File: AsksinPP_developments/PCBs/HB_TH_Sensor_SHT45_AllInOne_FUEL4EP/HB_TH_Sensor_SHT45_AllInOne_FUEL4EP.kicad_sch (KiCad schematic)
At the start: 41 parts, among them J1 Conn_01x03, J2 FTDI Debuger, J3 ISP Programmer, SW1 Config button, U1 ATmega1284P-AU, U2 TPS61221DCK, U3 SHT45-AD1B-R2

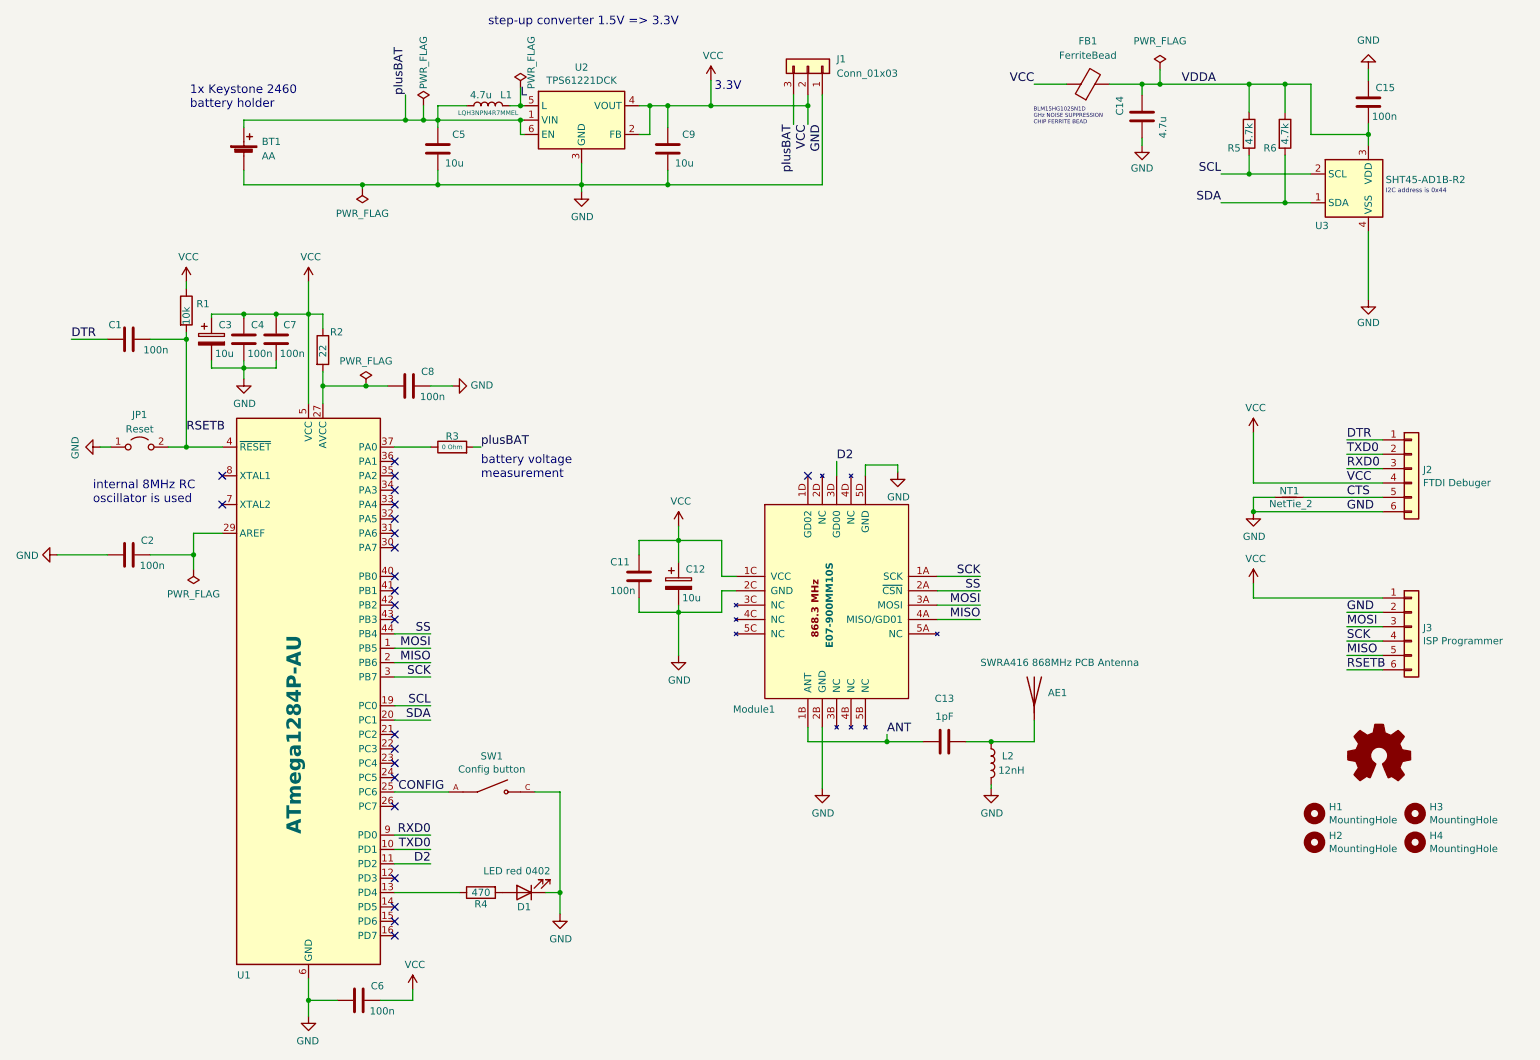
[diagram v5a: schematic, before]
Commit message: PCBs/HB_TH_Sensor_SHT45_AllInOne_FUEL4EP: Migration to KiCAD 8; improve solderability of RF module by hand
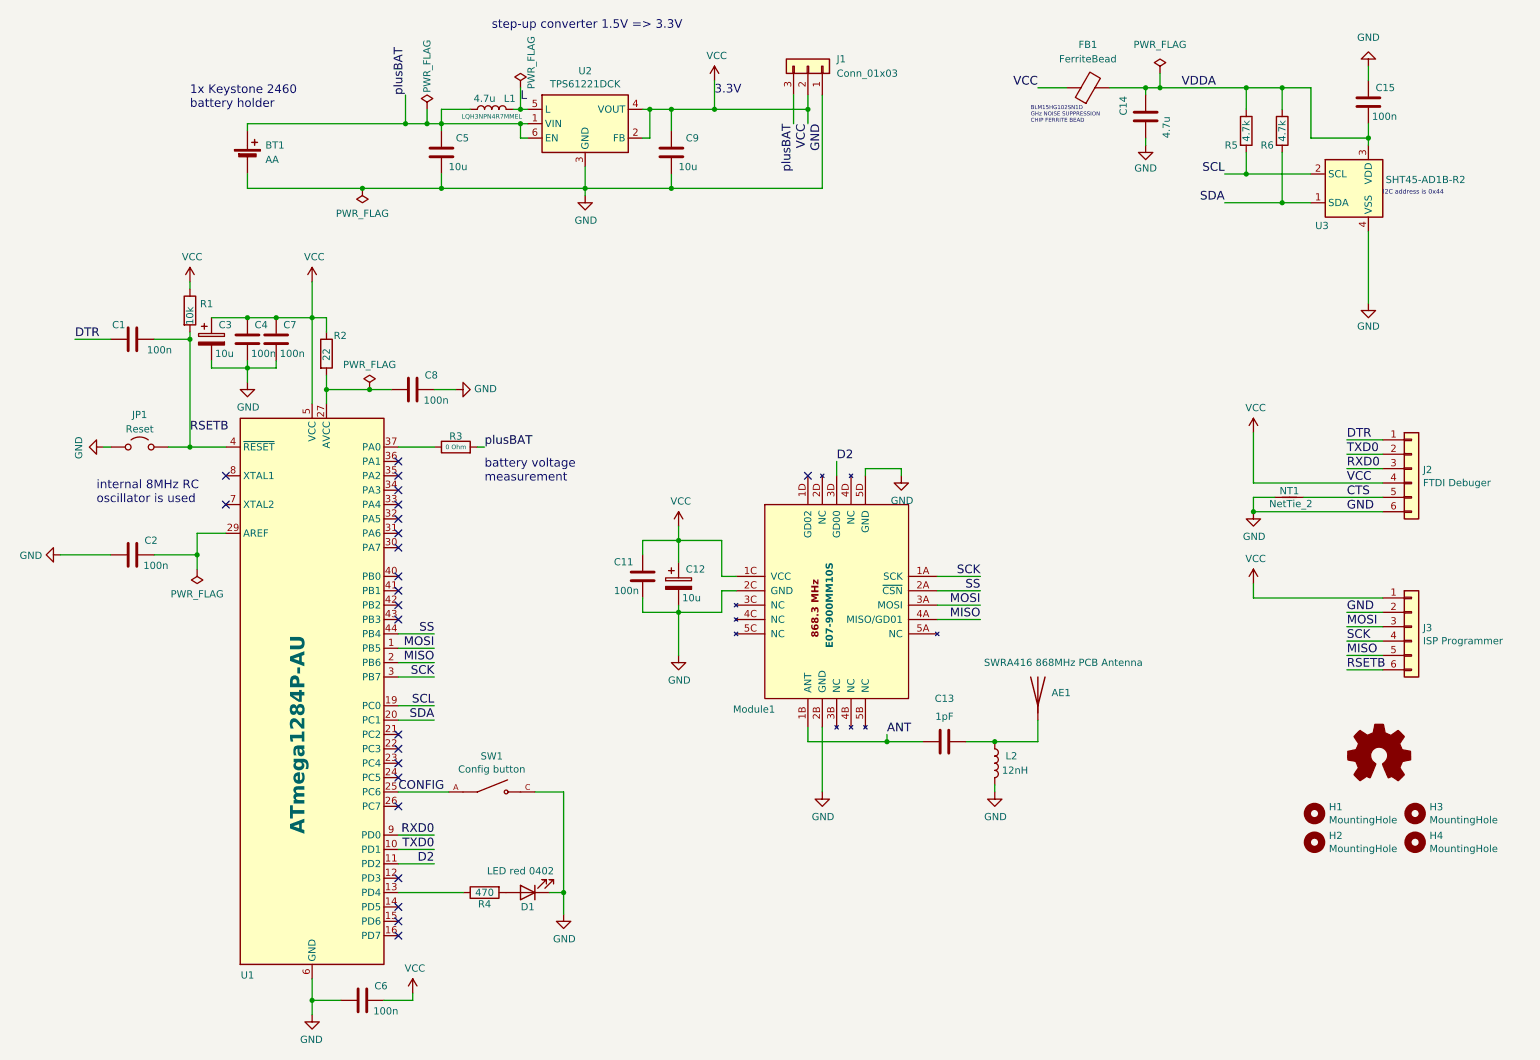
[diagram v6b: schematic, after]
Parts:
- AE1: footprint RF_Antenna:Texas_SWRA416_868MHz_915MHz -> FUEL4EP:Texas_SWRA416_868MHz_915MHz
- U3: footprint FUEL4EP:SHT4X -> Sensor_Humidity:Sensirion_DFN-4_1.5x1.5mm_P0.8mm_SHT4x_NoCentralPad
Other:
- moved on the sheet: AE1, BT1, C1, C11, C14, C2, C4, C5, C6, C8, C9, D1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

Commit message: PCB updates
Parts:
- U3: footprint Sensor_Humidity:Sensirion_DFN-4_1.5x1.5mm_P0.8mm_SHT4x_NoCentralPad -> FUEL4EP:Sensirion_DFN-4_1.5x1.5mm_P0.8mm_SHT4x_NoCentralPad; symbol Sensor_Humidity:SHT4x -> FUEL4EP:SHT4x
